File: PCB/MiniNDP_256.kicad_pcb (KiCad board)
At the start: 2 copper layers, 60 x 34 mm, 25 parts, among them J1 Conn_02x20_Odd_Even, U1 74161, U2 74161, U3 74161, U4 74138, U5 74374, U6 AS6C2008A, U7 741G32

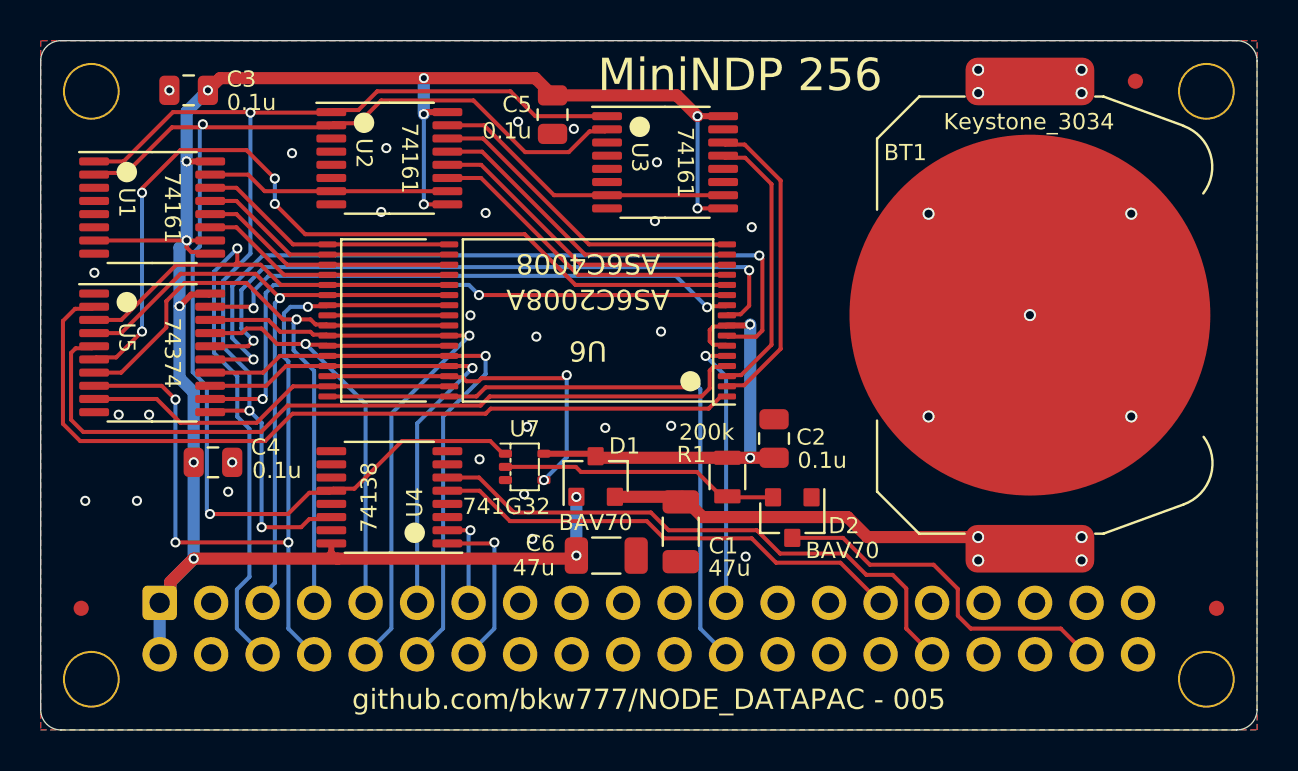
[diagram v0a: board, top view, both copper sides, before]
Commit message: readme, CR2016 and CR2012 battery holders
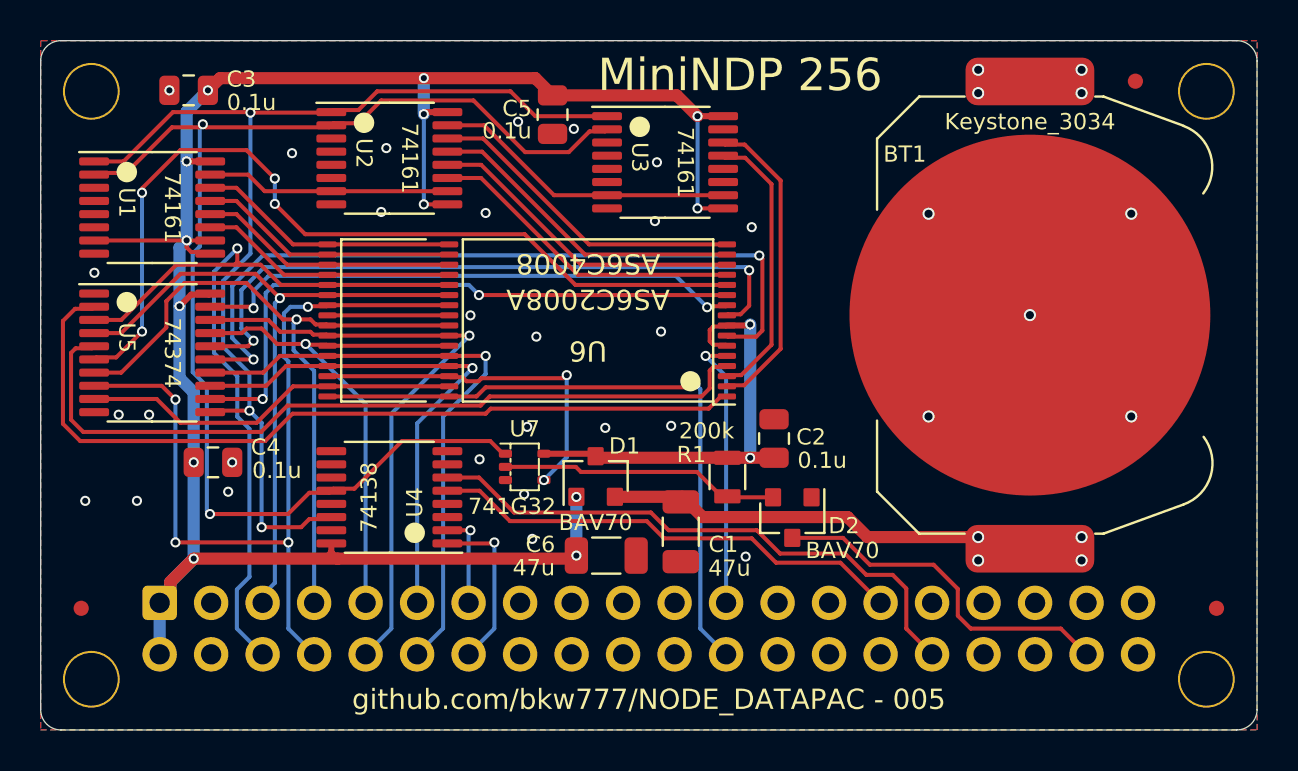
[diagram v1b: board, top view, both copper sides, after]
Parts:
- BT1: footprint 000_LOCAL:CR2032_holder_Keystone_3034 -> 000_LOCAL:Keystone_3028_3034
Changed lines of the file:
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@@
     (property "ki_keywords" "cap capacitor")
     (attr smd)
-    (fp_text reference "C6" (at -3.25 -0.6 unlocked) (layer "F.SilkS")
+    (fp_text reference "C6" (at -3.25 -0.55 unlocked) (layer "F.SilkS")
         (effects (font (size 0.8 0.8) (thickness 0.1)))
     )
@@
     (property "ki_keywords" "cap capacitor")
     (attr smd)
-    (fp_text reference "C2" (at 0.066 1.825 180) (layer "F.SilkS")
+    (fp_text reference "C2" (at 0.075 1.825 180) (layer "F.SilkS")
         (effects (font (size 0.8 0.8) (thickness 0.1)))
     )
@@
     (property "ki_keywords" "cap capacitor")
     (attr smd)
-    (fp_text reference "C1" (at 0.7 -2.1 unlocked) (layer "F.SilkS")
+    (fp_text reference "C1" (at 0.625 -2.1 unlocked) (layer "F.SilkS")
         (effects (font (size 0.8 0.8) (thickness 0.1)))
     )
@@
         (effects (font (size 0.8 0.8) (thickness 0.1)))
     )
-    (fp_text value "741G32" (at -0.9 1.95 unlocked) (layer "F.SilkS")
+    (fp_text value "741G32" (at -0.625 1.95 unlocked) (layer "F.SilkS")
         (effects (font (size 0.8 0.8) (thickness 0.1)))
     )
@@
         (effects (font (size 0.8 0.8) (thickness 0.1)))
     )
-    (fp_text value "200k" (at -2.2075 1.025) (layer "F.SilkS")
+    (fp_text value "200k" (at -2.275 1.025) (layer "F.SilkS")
         (effects (font (size 0.8 0.8) (thickness 0.1)))
     )
@@
       (net 1 "GND") (solder_mask_margin -0.1))
   )
-  (footprint "000_LOCAL:CR2032_holder_Keystone_3034" (layer "F.Cu")
+  (footprint "000_LOCAL:Keystone_3028_3034" (layer "F.Cu")
     (at 170.746 99.563 90)
     (descr "Keystone 3034 SMD battery holder for 2020, 2025 and 2032 coincell batteries. http://www.keyelco.com/product-pdf.cfm?p=798")
@@
     (property "ki_keywords" "battery cell")
     (attr smd)
-    (fp_text reference "BT1" (at 8.013 -6.146 180) (layer "F.SilkS")
-        (effects (font (size 0.8 0.8) (thickness 0.1)))
-    )
-    (fp_text value "Keystone_3034" (at 9.538 -0.046 180) (layer "F.SilkS")
+    (fp_text reference "BT1" (at 7.938 -6.171 180) (layer "F.SilkS")
+        (effects (font (size 0.8 0.8) (thickness 0.1)))
+    )
+    (fp_text value "Keystone_3034" (at 9.538 0.004 180) (layer "F.SilkS")
         (effects (font (size 0.8 0.8) (thickness 0.1)))
     )
@@
       (rotate (xyz 0 0 0))
     )
-    (model "${KIPRJMOD}/000_LOCAL.pretty/3dshapes/CR2032.step"
+    (model "${KIPRJMOD}/000_LOCAL.pretty/3dshapes/CR2016_holder_BAT-HLD-002-SMT.STEP" hide
+      (offset (xyz 0 0 0))
+      (scale (xyz 1 1 1))
+      (rotate (xyz -90 0 0))
+    )
+    (model "${KIPRJMOD}/000_LOCAL.pretty/3dshapes/CR2012_holder_Keystone_3028.step" hide
+      (offset (xyz 0 0 0))
+      (scale (xyz 1 1 1))
+      (rotate (xyz 0 0 90))
+    )
+    (model "${KIPRJMOD}/000_LOCAL.pretty/3dshapes/CR2012_blank.step" hide
+      (offset (xyz 0 0 1.2))
+      (scale (xyz 1 1 1))
+      (rotate (xyz 180 0 0))
+    )
+    (model "${KIPRJMOD}/000_LOCAL.pretty/3dshapes/CR2016_blank.step" hide
+      (offset (xyz 0 0 1.6))
+      (scale (xyz 1 1 1))
+      (rotate (xyz 180 0 0))
+    )
+    (model "${KIPRJMOD}/000_LOCAL.pretty/3dshapes/CR2032_blank.step"
       (offset (xyz 0 0 3.2))
       (scale (xyz 1 1 1))
-      (rotate (xyz 90 0 0))
+      (rotate (xyz 180 0 0))
     )
   )
@@
     (property "ki_keywords" "cap capacitor")
     (attr smd)
-    (fp_text reference "C5" (at -0.5 1.75) (layer "F.SilkS")
-        (effects (font (size 0.8 0.8) (thickness 0.1)))
-    )
+    (fp_text reference "C5" (at -0.3 1.75) (layer "F.SilkS")
+        (effects (font (size 0.8 0.8) (thickness 0.1)))
+    )

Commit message: convert wires to busses in bkw sch
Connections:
- D2 pad 1: unconnected-(D2-A-Pad1) -> /SLEEP
- D2 pad 2: /SLEEP -> unconnected-(D2-A-Pad2)
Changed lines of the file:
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@@
   (net 23 "/~{A}")
   (net 24 "/RAM_RST")
-  (net 25 "unconnected-(D2-A-Pad1)")
+  (net 25 "unconnected-(D2-A-Pad2)")
   (net 26 "unconnected-(J1-Pin_39-Pad39)")
   (net 27 "unconnected-(J1-Pin_40-Pad40)")
@@
       (stroke (width 0.1) (type solid)) (layer "F.Fab"))
     (pad "1" smd roundrect (at -1 -0.95 270) (size 0.9 0.8) (layers "F.Cu" "F.Paste" "F.Mask") (roundrect_rratio 0.1)
-      (net 25 "unconnected-(D2-A-Pad1)") (pinfunction "A") (pintype "passive+no_connect"))
+      (net 40 "/SLEEP") (pinfunction "A") (pintype "passive"))
     (pad "2" smd roundrect (at -1 0.95 270) (size 0.9 0.8) (layers "F.Cu" "F.Paste" "F.Mask") (roundrect_rratio 0.1)
-      (net 40 "/SLEEP") (pinfunction "A") (pintype "passive"))
+      (net 25 "unconnected-(D2-A-Pad2)") (pinfunction "A") (pintype "passive+no_connect"))
     (pad "3" smd roundrect (at 1 0 270) (size 0.9 0.8) (layers "F.Cu" "F.Paste" "F.Mask") (roundrect_rratio 0.1)
       (net 24 "/RAM_RST") (pinfunction "K") (pintype "passive"))

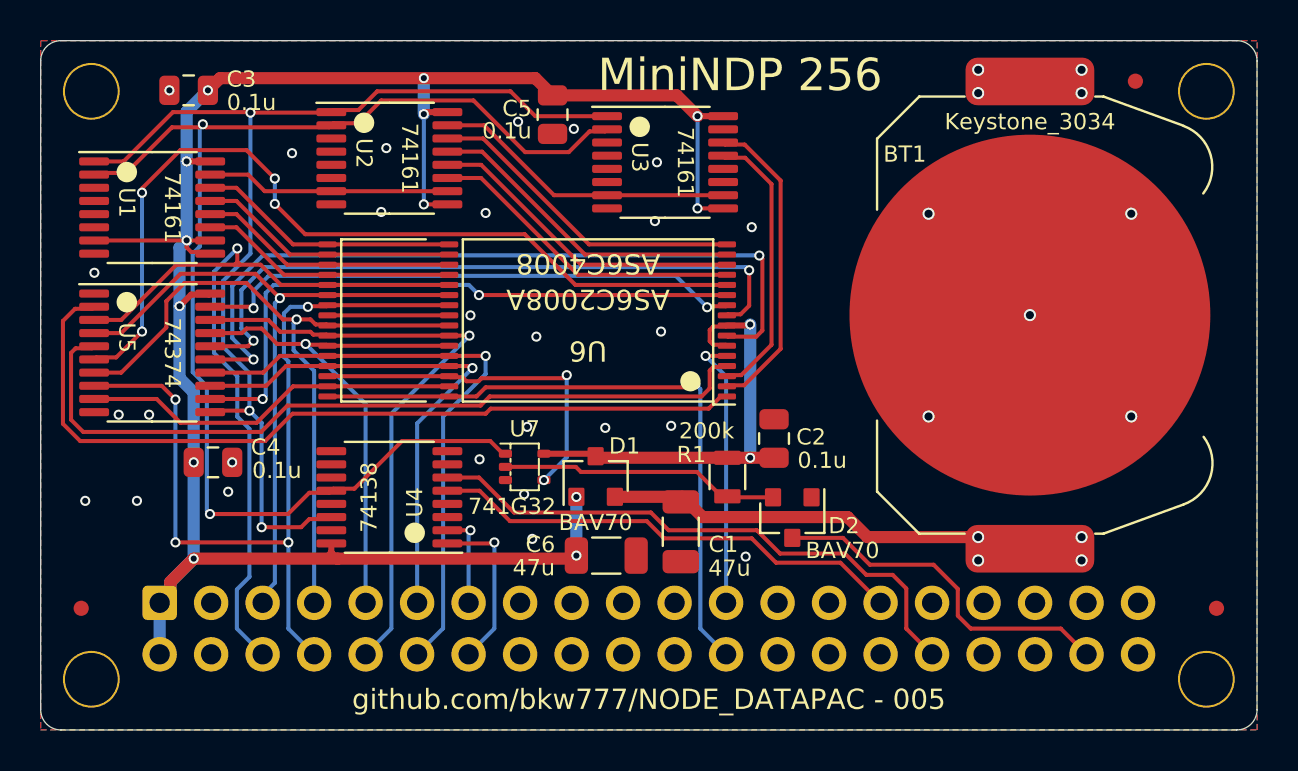
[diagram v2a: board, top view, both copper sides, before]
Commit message: minindp u7 footprint, 2 BAV70 -> 1 BAV70S
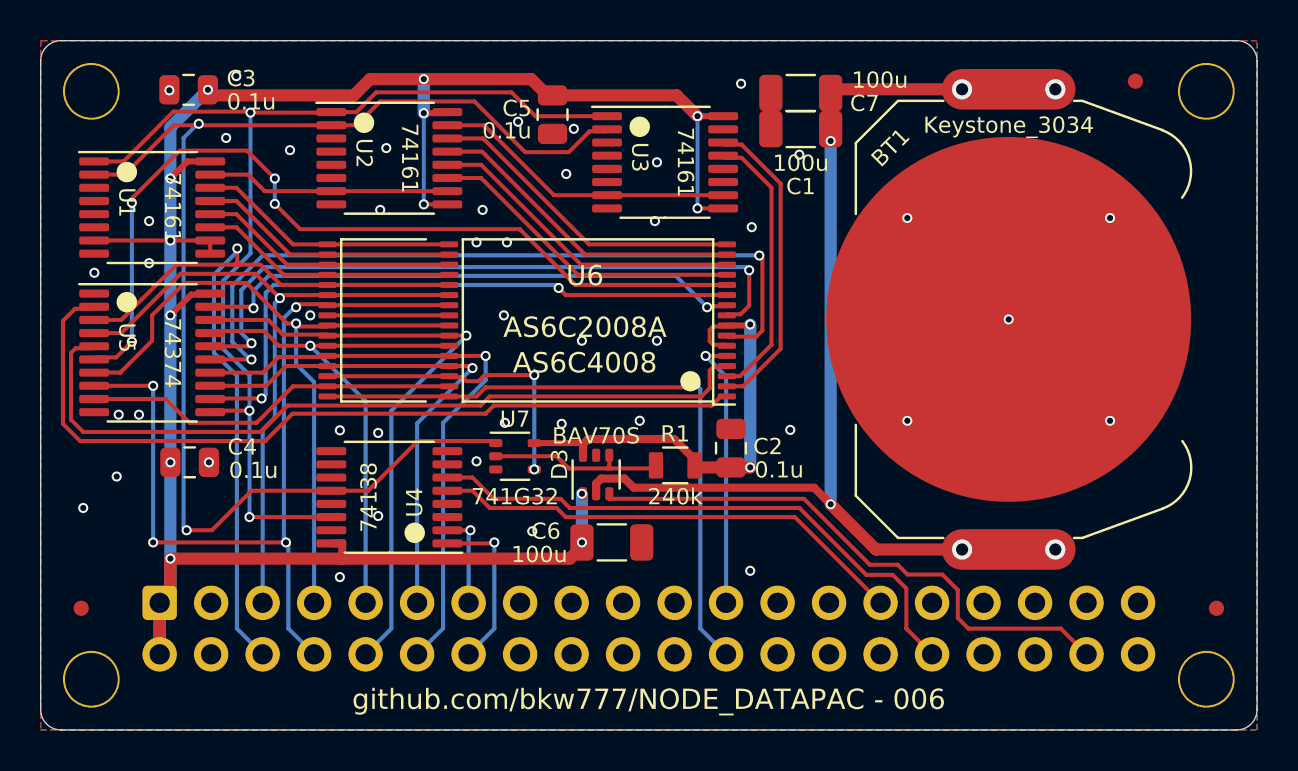
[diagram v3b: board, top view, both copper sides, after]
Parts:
- removed D1, D2: BAV70, 000_LOCAL:SOT-23
- added C7: 100u, 000_LOCAL:C_1206, F.Cu at (159.4, 88.6)
- added D3: BAV70S, 000_LOCAL:SOT-363_SC-70-6, F.Cu at (149.3, 107.4)
- C1, C6: value 47u -> 100u
- R1: value 200k -> 240k
- moved C1 20.7 mm to (159.4, 90.4), turned to 180 degrees
- moved R1 2.64 mm to (153.2, 107.0), turned to 180 degrees
- moved C2 2.18 mm to (156.0, 106.1)
- moved C4 1.15 mm to (129.3, 106.8)
- moved BT1 1.07 mm to (169.7, 99.8)
- moved U7 0.71 mm to (145.3, 106.5)
- moved C6 0.71 mm to (150.1, 110.8)
- renumbered REF** to F1, REF** to F2, REF** to F3, REF** to M1, REF** to M2, REF** to M3, REF** to M4
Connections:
- M1 pad : GND -> (no net)
- M2 pad : GND -> (no net)
- M3 pad : GND -> (no net)
- M4 pad : GND -> (no net)
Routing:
- net /BATT+: track 26.1 -> 51.5 mm, vias 8 -> 6
- net /RAM_RST: track 17.7 -> 27.8 mm
- net /SLEEP: track 13.8 -> 9.00 mm
- net VBUS: track 106.6 -> 110.3 mm
- net /~{CE}: track 17.7 -> 15.1 mm
- net /~{BYTE}: track 64.6 -> 66.0 mm
- net VMEM: track 21.7 -> 22.7 mm
- net /AD0: track 42.1 -> 41.6 mm
- net GND: vias 32 -> 45
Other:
- board text added: "MiniNDP 256"
- board text removed: "${TITLE}"

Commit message: pics
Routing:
- net GND: vias 45 -> 31
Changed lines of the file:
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@@
   )
   (segment (start 136.1 99.575) (end 142.1 99.575) (width 0.2) (layer "F.Cu") (net 1))
-  (via (at 136.71 112.485) (size 0.5) (drill 0.3) (layers "F.Cu" "B.Cu") (free) (net 1))
-  (via (at 136.71 105.246) (size 0.5) (drill 0.3) (layers "F.Cu" "B.Cu") (free) (net 1))
   (via (at 169.7 99.775) (size 0.5) (drill 0.3) (layers "F.Cu" "B.Cu") (net 1))
   (via (at 164.7 94.775) (size 0.5) (drill 0.3) (layers "F.Cu" "B.Cu") (net 1))
-  (via (at 143.75 94.375) (size 0.5) (drill 0.3) (layers "F.Cu" "B.Cu") (free) (net 1))
   (via (at 174.7 94.775) (size 0.5) (drill 0.3) (layers "F.Cu" "B.Cu") (net 1))
   (via (at 143.45 95.975) (size 0.5) (drill 0.3) (layers "F.Cu" "B.Cu") (free) (net 1))
-  (via (at 138.6 109.475) (size 0.5) (drill 0.3) (layers "F.Cu" "B.Cu") (free) (net 1))
-  (via (at 125.7 107.525) (size 0.5) (drill 0.3) (layers "F.Cu" "B.Cu") (free) (net 1))
+  (via (at 138.615 109.691) (size 0.5) (drill 0.3) (layers "F.Cu" "B.Cu") (free) (net 1))
   (via (at 152.35 92.025) (size 0.5) (drill 0.3) (layers "F.Cu" "B.Cu") (free) (net 1))
-  (via (at 144.85 104.875) (size 0.5) (drill 0.3) (layers "F.Cu" "B.Cu") (free) (net 1))
-  (via (at 157.025 95.225) (size 0.5) (drill 0.3) (layers "F.Cu" "B.Cu") (free) (net 1))
   (via (at 131.6 87.775) (size 0.5) (drill 0.3) (layers "F.Cu" "B.Cu") (free) (net 1))
   (via (at 135.25 99.575) (size 0.5) (drill 0.3) (layers "F.Cu" "B.Cu") (free) (net 1))
-  (via (at 124.05 109.075) (size 0.5) (drill 0.3) (layers "F.Cu" "B.Cu") (free) (net 1))
-  (via (at 144.8 99.575) (size 0.5) (drill 0.3) (layers "F.Cu" "B.Cu") (free) (net 1))
-  (via (at 147.875 92.6) (size 0.5) (drill 0.3) (layers "F.Cu" "B.Cu") (free) (net 1))
+  (via (at 124.8 108.525) (size 0.5) (drill 0.3) (layers "F.Cu" "B.Cu") (free) (net 1))
+  (via (at 134.3 91.475) (size 0.5) (drill 0.3) (layers "F.Cu" "B.Cu") (free) (net 1))
+  (via (at 145.35 99.475) (size 0.5) (drill 0.3) (layers "F.Cu" "B.Cu") (free) (net 1))
   (via (at 164.7 104.775) (size 0.5) (drill 0.3) (layers "F.Cu" "B.Cu") (net 1))
+  (via (at 131.05 90.825) (size 0.5) (drill 0.3) (layers "F.Cu" "B.Cu") (free) (net 1))
   (via (at 130.25 106.825) (size 0.5) (drill 0.3) (layers "F.Cu" "B.Cu") (free) (net 1))
   (via (at 144.95 95.975) (size 0.5) (drill 0.3) (layers "F.Cu" "B.Cu") (free) (net 1))
   (via (at 128.3 88.475) (size 0.5) (drill 0.3) (layers "F.Cu" "B.Cu") (net 1))
   (via (at 124.6 97.475) (size 0.5) (drill 0.3) (layers "F.Cu" "B.Cu") (free) (net 1))
-  (via (at 151.5 104.775) (size 0.5) (drill 0.3) (layers "F.Cu" "B.Cu") (free) (net 1))
   (via (at 158.925 105.225) (size 0.5) (drill 0.3) (layers "F.Cu" "B.Cu") (free) (net 1))
-  (via (at 126.8 104.475) (size 0.5) (drill 0.3) (layers "F.Cu" "B.Cu") (free) (net 1))
   (via (at 152.25 94.925) (size 0.5) (drill 0.3) (layers "F.Cu" "B.Cu") (free) (net 1))
-  (via (at 131.1 90.825) (size 0.5) (drill 0.3) (layers "F.Cu" "B.Cu") (free) (net 1))
-  (via (at 156.5 88.15) (size 0.5) (drill 0.3) (layers "F.Cu" "B.Cu") (free) (net 1))
-  (via (at 139 91.325) (size 0.5) (drill 0.3) (layers "F.Cu" "B.Cu") (free) (net 1))
-  (via (at 134.25 91.425) (size 0.5) (drill 0.3) (layers "F.Cu" "B.Cu") (free) (net 1))
   (via (at 147.65 104.925) (size 0.5) (drill 0.3) (layers "F.Cu" "B.Cu") (free) (net 1))
   (via (at 145.5 90.025) (size 0.5) (drill 0.3) (layers "F.Cu" "B.Cu") (net 1))
-  (via (at 138.6 105.375) (size 0.5) (drill 0.3) (layers "F.Cu" "B.Cu") (free) (net 1))
-  (via (at 148.25 90.375) (size 0.5) (drill 0.3) (layers "F.Cu" "B.Cu") (free) (net 1))
-  (via (at 159.375 91.65) (size 0.5) (drill 0.3) (layers "F.Cu" "B.Cu") (free) (net 1))
+  (via (at 138.615 105.754) (size 0.5) (drill 0.3) (layers "F.Cu" "B.Cu") (free) (net 1))
+  (via (at 130.25 108.825) (size 0.5) (drill 0.3) (layers "F.Cu" "B.Cu") (free) (net 1))
   (via (at 146.2 110.225) (size 0.5) (drill 0.3) (layers "F.Cu" "B.Cu") (free) (net 1))
-  (via (at 143.45 106.775) (size 0.5) (drill 0.3) (layers "F.Cu" "B.Cu") (free) (net 1))
-  (via (at 148.65 100.825) (size 0.5) (drill 0.3) (layers "F.Cu" "B.Cu") (free) (net 1))
-  (via (at 156.95 112.175) (size 0.5) (drill 0.3) (layers "F.Cu" "B.Cu") (free) (net 1))
+  (via (at 143.4 106.575) (size 0.5) (drill 0.3) (layers "F.Cu" "B.Cu") (free) (net 1))
+  (via (at 158.2 111.325) (size 0.5) (drill 0.3) (layers "F.Cu" "B.Cu") (free) (net 1))
   (via (at 174.7 104.775) (size 0.5) (drill 0.3) (layers "F.Cu" "B.Cu") (net 1))
-  (via (at 127.3 97) (size 0.5) (drill 0.3) (layers "F.Cu" "B.Cu") (free) (net 1))
-  (via (at 127.3 94.925) (size 0.5) (drill 0.3) (layers "F.Cu" "B.Cu") (free) (net 1))
+  (via (at 138.65 112.375) (size 0.5) (drill 0.3) (layers "F.Cu" "B.Cu") (free) (net 1))
   (via (at 138.7 94.375) (size 0.5) (drill 0.3) (layers "F.Cu" "B.Cu") (free) (net 1))
-  (via (at 152.35 100.825) (size 0.5) (drill 0.3) (layers "F.Cu" "B.Cu") (free) (net 1))
-  (via (at 125.8 104.475) (size 0.5) (drill 0.3) (layers "F.Cu" "B.Cu") (free) (net 1))
+  (via (at 151.2 100.875) (size 0.5) (drill 0.3) (layers "F.Cu" "B.Cu") (free) (net 1))
+  (via (at 126.15 104.475) (size 0.5) (drill 0.3) (layers "F.Cu" "B.Cu") (free) (net 1))
   (segment (start 154.95 100.3) (end 155.125 100.125) (width 0.2) (layer "F.Cu") (net 2))
   (segment (start 155.125 101.025) (end 154.95 100.85) (width 0.2) (layer "F.Cu") (net 2))
